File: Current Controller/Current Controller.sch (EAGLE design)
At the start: 15 parts, among them IC1 OP27, Q1 MJ11032, X1 22-23-2031, X2 22-23-2031, X3 1-227161-7, X4 GMSTBA2

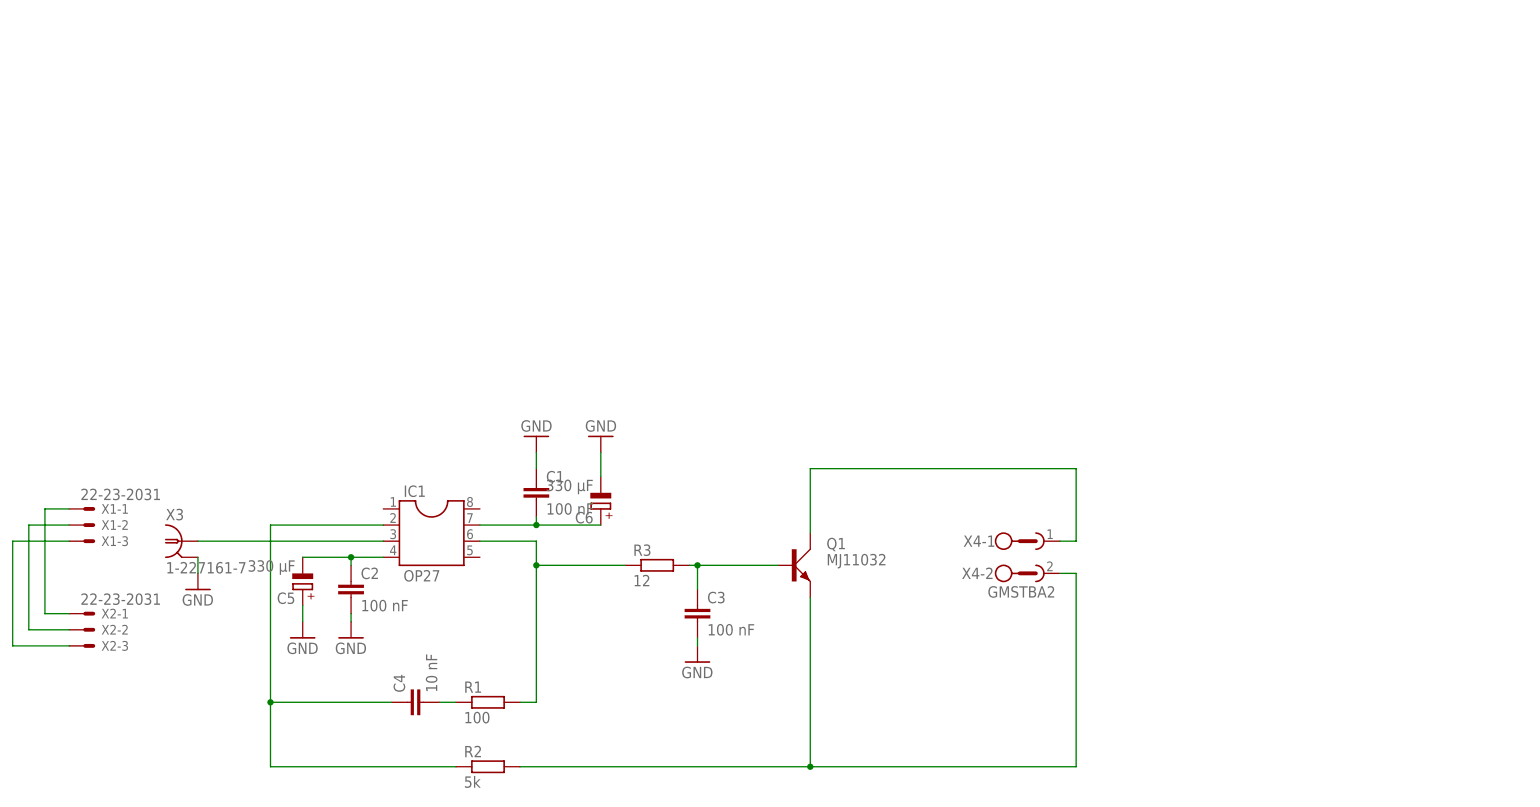
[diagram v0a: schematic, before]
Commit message: Add files via upload
Placed the shunt resistor directly on the board, and did some minor bugfixes
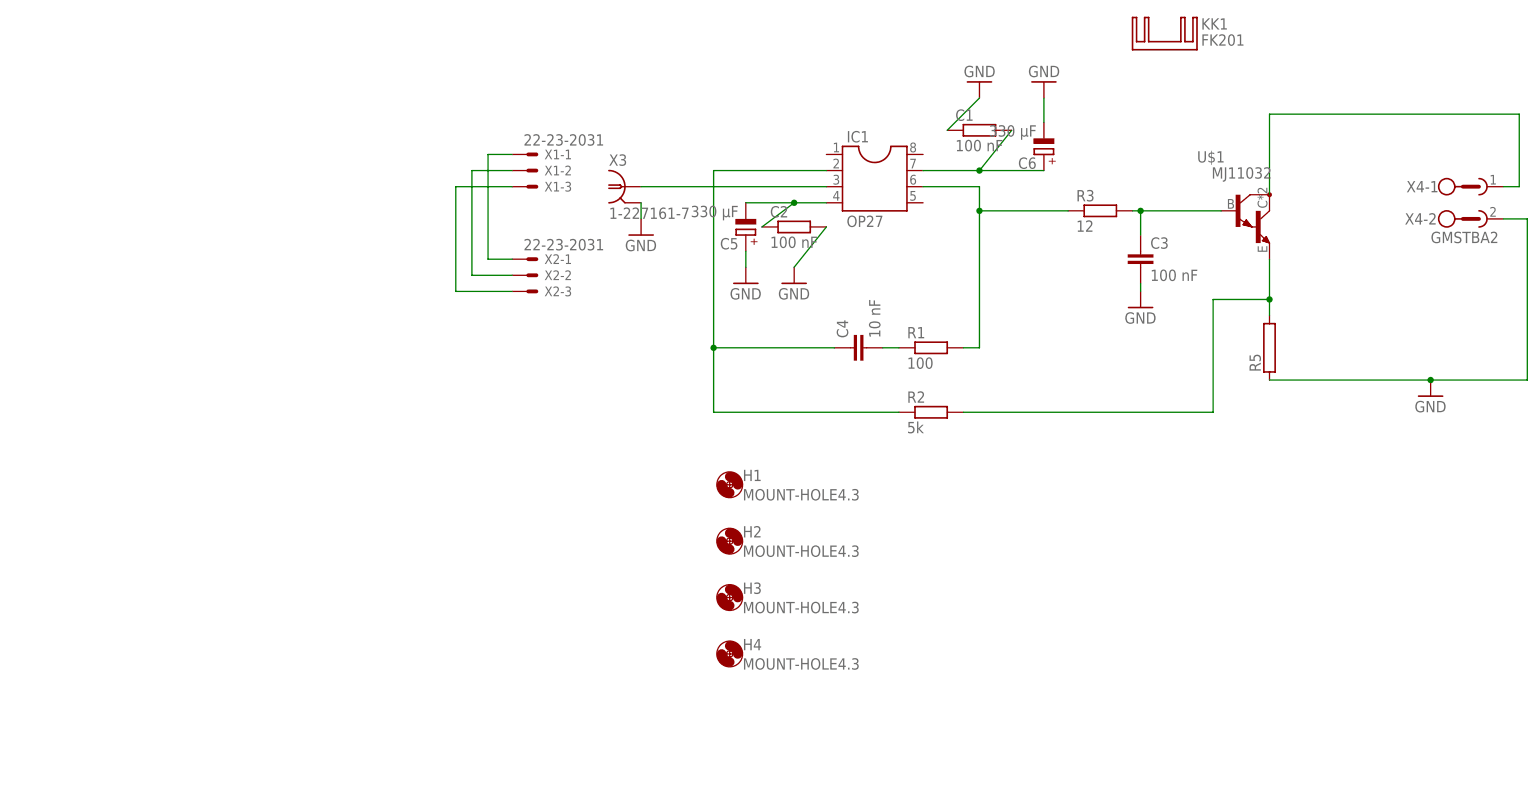
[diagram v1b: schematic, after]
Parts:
- removed Q1: MJ11032, transistor-power:2N3055
- added H1, H2, H3, H4: MOUNT-HOLE4.3, holes:MOUNT-HOLE4.3
- added KK1: FK201, heatsink:FK201
- added R5: (no value), resistor-power:RRWM10X64
- added U$1: MJ11032, Current Controller:MJ11032
- C1, C2: device resistor:C-EU025-050X050 -> rcl:R-EU_M1206
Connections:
- removed net CURRENT_OUT: Q1.E, R2.2, X4-2.1
- new net N$3: R2.2, R5.2, U$1.E
- net BASE_VOLTAGE: now also U$1.B; no longer Q1.B
- net CURRENT_IN: now also U$1.C; no longer Q1.C
- net GND: now also R5.1, X4-2.1
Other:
- moved on the sheet: C1, C2, C3, C4, C5, C6, IC1, R1, R2, R3, X1-1, X1-2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
